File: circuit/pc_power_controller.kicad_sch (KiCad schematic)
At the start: 7 parts, among them J1 PWR_SW_HEADER, J2 PLED_HEADER, U1 TLP225A(F), U2 TLP621-1, U3 Seeed_XIAO_ESP32C3

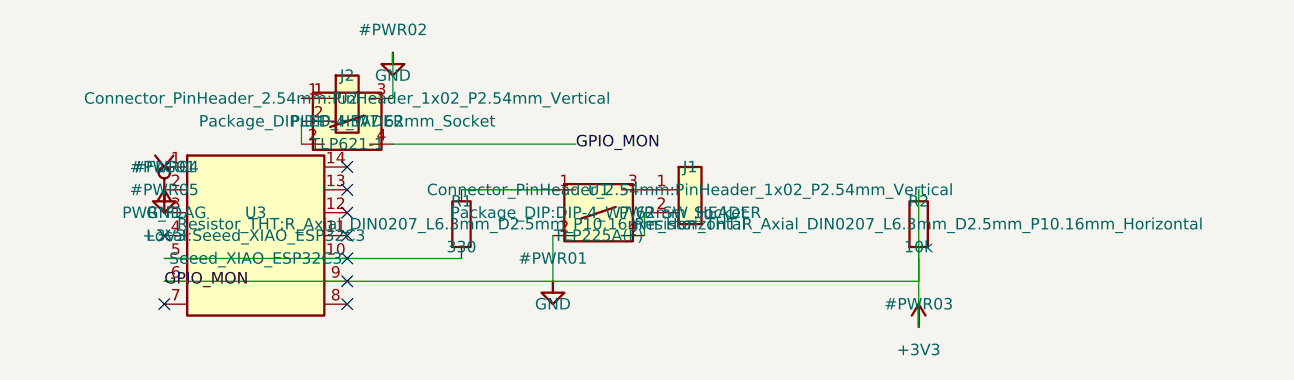
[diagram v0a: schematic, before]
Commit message: fix: correct XIAO pin mapping, clean up schematic wiring, add ESPHome firmware
- Fix Seeed XIAO ESP32C3 pad/pin mapping in schematic symbol, footprint,
  and PCB net assignment (5V/GND/3V3 physically sit at the end of the
  right pin column, not the start of the left column as first assumed).
- Rewrite schematic wiring to use net labels for all inter-component
  signals instead of long routed wires across the page; fixes a real bug
  where a 3V3 wire crossed through the GPIO_MON label stub and merged
  the two nets.
- Add ESPHome firmware (esphome/) for the XIAO ESP32C3: momentary PWR_SW
  pulse button, separate forced-power-off button/script, and PLED
  blink/on/off detection via a single gpio binary_sensor (pulse_counter
  was removed since ESPHome can't share one pin across two components).

Co-Authored-By: Claude Sonnet 5 <noreply@anthropic.com>
Claude-Session: https://claude.ai/code/session_017SHrsAt73jUX19kpfbZs3f
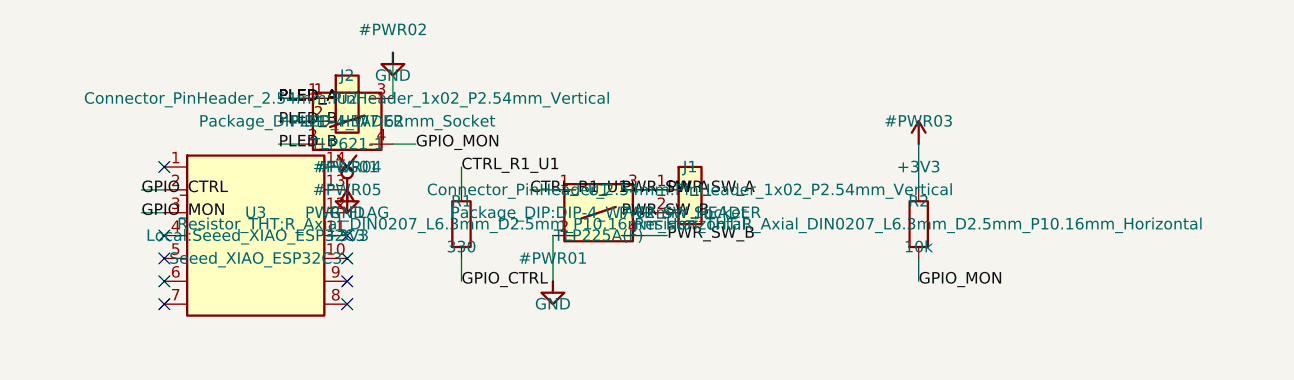
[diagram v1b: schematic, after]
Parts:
- U3: Note Seeed Studio XIAO ESP32C3, mounted on 2x7 2.54mm female headers. Pin5=D1/GPIO3 (relay control out), Pin6=D2/GPIO4 (PLED monitor in) -> Seeed Studio XIAO ESP32C3, mounted on 2x7 2.54mm female headers. Pin2=D1/GPIO3 (relay control out), Pin3=D2/GPIO4 (PLED monitor in). Pin order matches Seeed's real silkscreen: left column D0-D6 (pins 1-7), right column D7-D10,3V3,GND,5V (pins 8-14)
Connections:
- net +3V3: now also U3.12 (3V3); no longer R2.2, U2.4, U3.3 (3V3), U3.6 (D2/GPIO4)
- net GND: now also U3.13 (GND); no longer U3.2 (GND)
- net CTRL_R1_U1: now reaches R1.1, U1.1
- net PWR_SW_A: now reaches J1.1 (Pin_1), U1.3
- net PWR_SW_B: now reaches J1.2 (Pin_2), U1.4
- net PLED_A: now reaches J2.1 (Pin_1), U2.1
- net PLED_B: now reaches J2.2 (Pin_2), U2.2
- net at U3.5 (D4/GPIO6): no longer R1.2
- new net GPIO_CTRL: R1.2, U3.2 (D1/GPIO3)
- new net GPIO_MON: R2.2, U2.4, U3.3 (D2/GPIO4)
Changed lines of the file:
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@@
     (pin "2")
   )
-  (symbol (lib_id "power:+3V3") (at 88.9 45.72 0) (unit 1)
-    (in_bom no) (on_board no)
-    (property "Reference" "#PWR03" (at 88.9 43.18 0)
-      (effects (font (size 1.27 1.27)))
-    )
-    (property "Value" "+3V3" (at 88.9 48.26 0)
-      (effects (font (size 1.27 1.27)))
-    )
-    (property "Footprint" "" (at 88.9 45.72 0)
-      (effects (font (size 1.27 1.27)) hide)
-    )
-    (property "Datasheet" "" (at 88.9 45.72 0)
+  (symbol (lib_id "power:+3V3") (at 88.9 25.4 0) (unit 1)
+    (in_bom no) (on_board no)
+    (property "Reference" "#PWR03" (at 88.9 22.86 0)
+      (effects (font (size 1.27 1.27)))
+    )
+    (property "Value" "+3V3" (at 88.9 27.939999999999998 0)
+      (effects (font (size 1.27 1.27)))
+    )
+    (property "Footprint" "" (at 88.9 25.4 0)
+      (effects (font (size 1.27 1.27)) hide)
+    )
+    (property "Datasheet" "" (at 88.9 25.4 0)
       (effects (font (size 1.27 1.27)) hide)
     )
@@
       (effects (font (size 1.27 1.27)) hide)
     )
-    (property "Note" "Seeed Studio XIAO ESP32C3, mounted on 2x7 2.54mm female headers. Pin5=D1/GPIO3 (relay control out), Pin6=D2/GPIO4 (PLED monitor in)" (at 15.24 35.56 0)
+    (property "Note" "Seeed Studio XIAO ESP32C3, mounted on 2x7 2.54mm female headers. Pin2=D1/GPIO3 (relay control out), Pin3=D2/GPIO4 (PLED monitor in). Pin order matches Seeed's real silkscreen: left column D0-D6 (pins 1-7), right column D7-D10,3V3,GND,5V (pins 8-14)" (at 15.24 35.56 0)
       (effects (font (size 1.27 1.27)) hide)
     )
@@
     (pin "14")
   )
-  (symbol (lib_id "power:GND") (at 5.08 30.48 0) (unit 1)
-    (in_bom no) (on_board no)
-    (property "Reference" "#PWR04" (at 5.08 27.94 0)
-      (effects (font (size 1.27 1.27)))
-    )
-    (property "Value" "GND" (at 5.08 33.02 0)
-      (effects (font (size 1.27 1.27)))
-    )
-    (property "Footprint" "" (at 5.08 30.48 0)
-      (effects (font (size 1.27 1.27)) hide)
-    )
-    (property "Datasheet" "" (at 5.08 30.48 0)
-      (effects (font (size 1.27 1.27)) hide)
-    )
-    (pin "1")
-  )
-  (symbol (lib_id "power:+3V3") (at 5.08 33.02 0) (unit 1)
-    (in_bom no) (on_board no)
-    (property "Reference" "#PWR05" (at 5.08 30.480000000000004 0)
-      (effects (font (size 1.27 1.27)))
-    )
-    (property "Value" "+3V3" (at 5.08 35.56 0)
-      (effects (font (size 1.27 1.27)))
-    )
-    (property "Footprint" "" (at 5.08 33.02 0)
-      (effects (font (size 1.27 1.27)) hide)
-    )
-    (property "Datasheet" "" (at 5.08 33.02 0)
-      (effects (font (size 1.27 1.27)) hide)
-    )
-    (pin "1")
-  )
-  (symbol (lib_id "power:PWR_FLAG") (at 5.08 30.48 0) (unit 1)
-    (in_bom no) (on_board no)
-    (property "Reference" "#FLG01" (at 5.08 27.94 0)
-      (effects (font (size 1.27 1.27)))
-    )
-    (property "Value" "PWR_FLAG" (at 5.08 33.02 0)
-      (effects (font (size 1.27 1.27)))
-    )
-    (property "Footprint" "" (at 5.08 30.48 0)
-      (effects (font (size 1.27 1.27)) hide)
-    )
-    (property "Datasheet" "" (at 5.08 30.48 0)
-      (effects (font (size 1.27 1.27)) hide)
-    )
-    (pin "1")
-  )
-  (wire (pts (xy 5.08 38.1) (xy 38.1 38.1))
-    (stroke (width 0) (type default))
-  )
-  (wire (pts (xy 38.1 30.48) (xy 48.260000000000005 30.48))
-    (stroke (width 0) (type default))
-  )
-  (wire (pts (xy 48.260000000000005 30.48) (xy 48.260000000000005 30.480000000000004))
-    (stroke (width 0) (type default))
+  (symbol (lib_id "power:GND") (at 25.4 30.48 0) (unit 1)
+    (in_bom no) (on_board no)
+    (property "Reference" "#PWR04" (at 25.4 27.94 0)
+      (effects (font (size 1.27 1.27)))
+    )
+    (property "Value" "GND" (at 25.4 33.02 0)
+      (effects (font (size 1.27 1.27)))
+    )
+    (property "Footprint" "" (at 25.4 30.48 0)
+      (effects (font (size 1.27 1.27)) hide)
+    )
+    (property "Datasheet" "" (at 25.4 30.48 0)
+      (effects (font (size 1.27 1.27)) hide)
+    )
+    (pin "1")
+  )
+  (symbol (lib_id "power:+3V3") (at 25.4 33.02 0) (unit 1)
+    (in_bom no) (on_board no)
+    (property "Reference" "#PWR05" (at 25.4 30.480000000000004 0)
+      (effects (font (size 1.27 1.27)))
+    )
+    (property "Value" "+3V3" (at 25.4 35.56 0)
+      (effects (font (size 1.27 1.27)))
+    )
+    (property "Footprint" "" (at 25.4 33.02 0)
+      (effects (font (size 1.27 1.27)) hide)
+    )
+    (property "Datasheet" "" (at 25.4 33.02 0)
+      (effects (font (size 1.27 1.27)) hide)
+    )
+    (pin "1")
+  )
+  (symbol (lib_id "power:PWR_FLAG") (at 25.4 30.48 0) (unit 1)
+    (in_bom no) (on_board no)
+    (property "Reference" "#FLG01" (at 25.4 27.94 0)
+      (effects (font (size 1.27 1.27)))
+    )
+    (property "Value" "PWR_FLAG" (at 25.4 33.02 0)
+      (effects (font (size 1.27 1.27)))
+    )
+    (property "Footprint" "" (at 25.4 30.48 0)
+      (effects (font (size 1.27 1.27)) hide)
+    )
+    (property "Datasheet" "" (at 25.4 30.48 0)
+      (effects (font (size 1.27 1.27)) hide)
+    )
+    (pin "1")
+  )
+  (wire (pts (xy 5.08 30.480000000000004) (xy 2.54 30.480000000000004))
+    (stroke (width 0) (type default))
+  )
+  (label "GPIO_CTRL" (at 2.54 30.480000000000004 0)
+    (effects (font (size 1.27 1.27)) (justify left))
+  )
+  (wire (pts (xy 38.1 38.1) (xy 38.1 40.64))
+    (stroke (width 0) (type default))
+  )
+  (label "GPIO_CTRL" (at 38.1 40.64 0)
+    (effects (font (size 1.27 1.27)) (justify left))
+  )
+  (wire (pts (xy 38.1 30.48) (xy 38.1 27.94))
+    (stroke (width 0) (type default))
+  )
+  (label "CTRL_R1_U1" (at 38.1 27.94 0)
+    (effects (font (size 1.27 1.27)) (justify left))
+  )
+  (wire (pts (xy 48.260000000000005 30.480000000000004) (xy 45.720000000000006 30.480000000000004))
+    (stroke (width 0) (type default))
+  )
+  (label "CTRL_R1_U1" (at 45.720000000000006 30.480000000000004 0)
+    (effects (font (size 1.27 1.27)) (justify left))
   )
   (wire (pts (xy 48.260000000000005 35.56) (xy 48.26 35.56))
@@
     (stroke (width 0) (type default))
   )
-  (wire (pts (xy 58.42 30.480000000000004) (xy 58.42 30.48))
-    (stroke (width 0) (type default))
-  )
-  (wire (pts (xy 58.42 35.56) (xy 58.42 33.02))
-    (stroke (width 0) (type default))
-  )
-  (wire (pts (xy 20.32 20.32) (xy 20.32 20.32))
-    (stroke (width 0) (type default))
-  )
-  (wire (pts (xy 20.32 22.86) (xy 20.32 25.4))
-    (stroke (width 0) (type default))
+  (wire (pts (xy 58.42 30.480000000000004) (xy 60.96 30.480000000000004))
+    (stroke (width 0) (type default))
+  )
+  (label "PWR_SW_A" (at 60.96 30.480000000000004 0)
+    (effects (font (size 1.27 1.27)) (justify left))
+  )
+  (wire (pts (xy 58.42 30.48) (xy 55.88 30.48))
+    (stroke (width 0) (type default))
+  )
+  (label "PWR_SW_A" (at 55.88 30.48 0)
+    (effects (font (size 1.27 1.27)) (justify left))
+  )
+  (wire (pts (xy 58.42 35.56) (xy 60.96 35.56))
+    (stroke (width 0) (type default))
+  )
+  (label "PWR_SW_B" (at 60.96 35.56 0)
+    (effects (font (size 1.27 1.27)) (justify left))
+  )
+  (wire (pts (xy 58.42 33.02) (xy 55.88 33.02))
+    (stroke (width 0) (type default))
+  )
+  (label "PWR_SW_B" (at 55.88 33.02 0)
+    (effects (font (size 1.27 1.27)) (justify left))
+  )
+  (wire (pts (xy 20.32 20.32) (xy 17.78 20.32))
+    (stroke (width 0) (type default))
+  )
+  (label "PLED_A" (at 17.78 20.32 0)
+    (effects (font (size 1.27 1.27)) (justify left))
+  )
+  (wire (pts (xy 20.32 20.32) (xy 17.78 20.32))
+    (stroke (width 0) (type default))
+  )
+  (label "PLED_A" (at 17.78 20.32 0)
+    (effects (font (size 1.27 1.27)) (justify left))
+  )
+  (wire (pts (xy 20.32 22.86) (xy 17.78 22.86))
+    (stroke (width 0) (type default))
+  )
+  (label "PLED_B" (at 17.78 22.86 0)
+    (effects (font (size 1.27 1.27)) (justify left))
+  )
+  (wire (pts (xy 20.32 25.4) (xy 17.78 25.4))
+    (stroke (width 0) (type default))
+  )
+  (label "PLED_B" (at 17.78 25.4 0)
+    (effects (font (size 1.27 1.27)) (justify left))
   )
   (wire (pts (xy 30.479999999999997 20.32) (xy 30.48 20.32))
@@
     (stroke (width 0) (type default))
   )
-  (wire (pts (xy 30.479999999999997 25.4) (xy 50.8 25.4))
-    (stroke (width 0) (type default))
-  )
-  (label "GPIO_MON" (at 50.8 25.4 0)
-    (effects (font (size 1.27 1.27)) (justify left))
-  )
-  (wire (pts (xy 5.08 40.64) (xy 88.9 40.64))
-    (stroke (width 0) (type default))
-  )
-  (wire (pts (xy 88.9 40.64) (xy 88.9 38.1))
-    (stroke (width 0) (type default))
-  )
-  (label "GPIO_MON" (at 5.08 40.64 0)
-    (effects (font (size 1.27 1.27)) (justify left))
-  )
-  (wire (pts (xy 88.9 30.48) (xy 88.9 45.72))
+  (wire (pts (xy 30.479999999999997 25.4) (xy 33.019999999999996 25.4))
+    (stroke (width 0) (type default))
+  )
+  (label "GPIO_MON" (at 33.019999999999996 25.4 0)
+    (effects (font (size 1.27 1.27)) (justify left))
+  )
+  (wire (pts (xy 88.9 38.1) (xy 88.9 40.64))
+    (stroke (width 0) (type default))
+  )
+  (label "GPIO_MON" (at 88.9 40.64 0)
+    (effects (font (size 1.27 1.27)) (justify left))
+  )
+  (wire (pts (xy 5.08 33.02) (xy 2.54 33.02))
+    (stroke (width 0) (type default))
+  )
+  (label "GPIO_MON" (at 2.54 33.02 0)
+    (effects (font (size 1.27 1.27)) (justify left))
+  )
+  (wire (pts (xy 88.9 30.48) (xy 88.9 25.4))
     (stroke (width 0) (type default))
   )
@@
   (no_connect (at 5.08 35.56)
   )
+  (no_connect (at 5.08 38.1)
+  )
+  (no_connect (at 5.08 40.64)
+  )
   (no_connect (at 5.08 43.18)
   )
@@
   (no_connect (at 25.4 35.56)
   )
-  (no_connect (at 25.4 33.02)
-  )
-  (no_connect (at 25.4 30.480000000000004)
-  )
   (no_connect (at 25.4 27.94)
